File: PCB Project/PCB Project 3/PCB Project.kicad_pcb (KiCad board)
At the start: 2 copper layers, 80 x 60 mm, 25 parts, among them J1 Conn_01x03_Pin, J2 Conn_01x02_Pin, J3 Conn_01x02_Pin, U1 TL084, U2 TL084

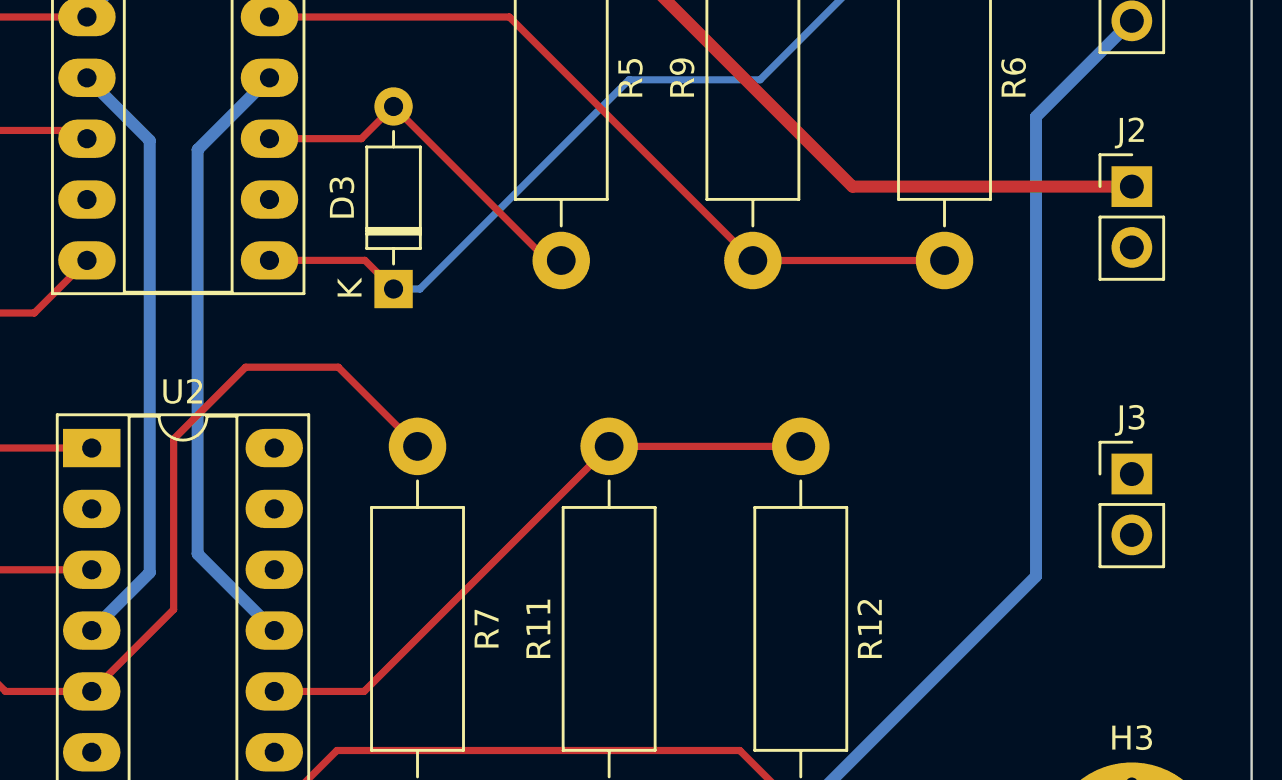
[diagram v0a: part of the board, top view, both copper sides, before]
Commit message: Added traces to power the IC Chips.
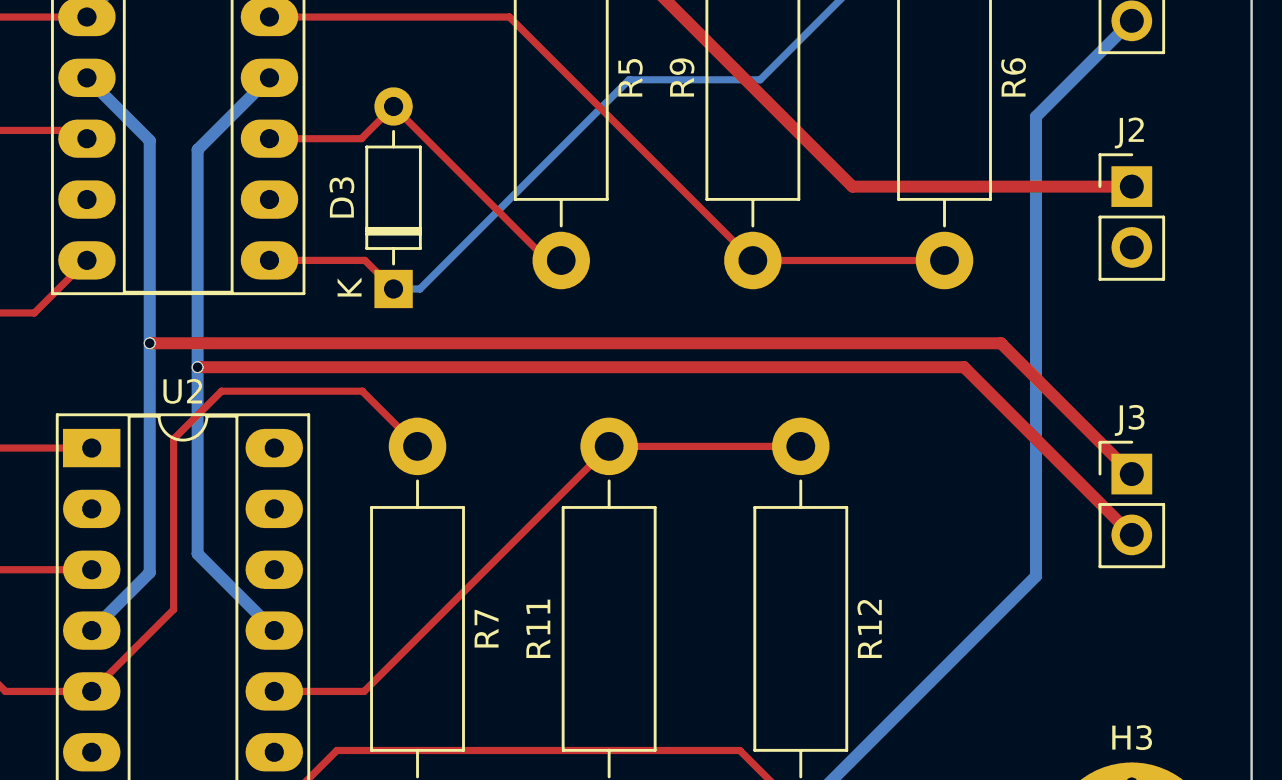
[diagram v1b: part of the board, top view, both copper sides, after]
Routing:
- net VCC: track 25.2 -> 68.4 mm, vias 0 -> 1
- net VDD: track 25.6 -> 67.5 mm, vias 0 -> 1
- net Net-(D4-K): track 30.9 -> 30.1 mm
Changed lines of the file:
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@@
   (segment (start 214.18 102.115) (end 220.61 108.545) (width 0.3) (layer "F.Cu") (net 6))
   (segment (start 220.61 108.545) (end 221.18 108.545) (width 0.3) (layer "F.Cu") (net 6))
-  (segment (start 211.875 113) (end 208 113) (width 0.3) (layer "F.Cu") (net 7))
-  (segment (start 208 113) (end 205 116) (width 0.3) (layer "F.Cu") (net 7))
   (segment (start 205 116) (end 205 123.115) (width 0.3) (layer "F.Cu") (net 7))
   (segment (start 197.98 126.535) (end 196.18 124.735) (width 0.3) (layer "F.Cu") (net 7))
-  (segment (start 215.18 116.305) (end 211.875 113) (width 0.3) (layer "F.Cu") (net 7))
+  (segment (start 205 123.115) (end 201.58 126.535) (width 0.3) (layer "F.Cu") (net 7))
   (segment (start 201.58 126.535) (end 197.98 126.535) (width 0.3) (layer "F.Cu") (net 7))
-  (segment (start 205 123.115) (end 201.58 126.535) (width 0.3) (layer "F.Cu") (net 7))
+  (segment (start 215.18 116.305) (end 212.875 114) (width 0.3) (layer "F.Cu") (net 7))
+  (segment (start 207 114) (end 205 116) (width 0.3) (layer "F.Cu") (net 7))
+  (segment (start 212.875 114) (end 207 114) (width 0.3) (layer "F.Cu") (net 7))
   (segment (start 196.18 117.115) (end 189.99 117.115) (width 0.3) (layer "F.Cu") (net 8))
   (segment (start 201.58 116.375) (end 196.92 116.375) (width 0.3) (layer "F.Cu") (net 8))
@@
   (segment (start 209.2 126.535) (end 212.95 126.535) (width 0.3) (layer "F.Cu") (net 18))
   (segment (start 223.18 116.305) (end 231.18 116.305) (width 0.3) (layer "F.Cu") (net 18))
+  (segment (start 239.54 112) (end 245 117.46) (width 0.5) (layer "F.Cu") (net 19))
+  (segment (start 204 112) (end 239.54 112) (width 0.5) (layer "F.Cu") (net 19))
+  (via (at 204 112) (size 0.5) (drill 0.4) (layers "F.Cu" "B.Cu") (net 19))
   (segment (start 204 121.575) (end 204 103.54) (width 0.5) (layer "B.Cu") (net 19))
   (segment (start 201.58 123.995) (end 204 121.575) (width 0.5) (layer "B.Cu") (net 19))
   (segment (start 204 103.54) (end 201.38 100.92) (width 0.5) (layer "B.Cu") (net 19))
+  (segment (start 206 113) (end 238 113) (width 0.5) (layer "F.Cu") (net 20))
+  (segment (start 238 113) (end 245 120) (width 0.5) (layer "F.Cu") (net 20))
+  (via (at 206 113) (size 0.5) (drill 0.4) (layers "F.Cu" "B.Cu") (net 20))
+  (segment (start 206 113) (end 206 103.92) (width 0.5) (layer "B.Cu") (net 20))
+  (segment (start 206 120.795) (end 209.2 123.995) (width 0.5) (layer "B.Cu") (net 20))
+  (segment (start 206 113) (end 206 120.795) (width 0.5) (layer "B.Cu") (net 20))
   (segment (start 206 103.92) (end 209 100.92) (width 0.5) (layer "B.Cu") (net 20))
-  (segment (start 209.2 123.995) (end 206 120.795) (width 0.5) (layer "B.Cu") (net 20))
-  (segment (start 206 120.795) (end 206 103.92) (width 0.5) (layer "B.Cu") (net 20))
   (zone (net 12) (net_name "GND") (layer "B.Cu") (hatch edge 0.5)
     (connect_pads (clearance 0.5))
